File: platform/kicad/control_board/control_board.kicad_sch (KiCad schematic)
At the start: 39 parts, among them IC1 Adafruit_HUZZAH_ESP, J1 DHT22, J1 PoE 1, J1 RJ45 IN - 1, J10 USB_PWR_IN, J11 Barrel_Jack, J2 DS18B20, J2 PoE 2, J2 RJ45 IN - 2, J3 PoE 3, J3 RJ45 IN - 3, J3 Sensor1, J4 Sensor2, J6 24V IN, J7 24V/5V OUT, J8 Nav Light, K1 LCA717, K2 LCA717, K3 LCA717, K4 LCA717, M1 STEPDOWN->5V, U1 USB_A_2.0

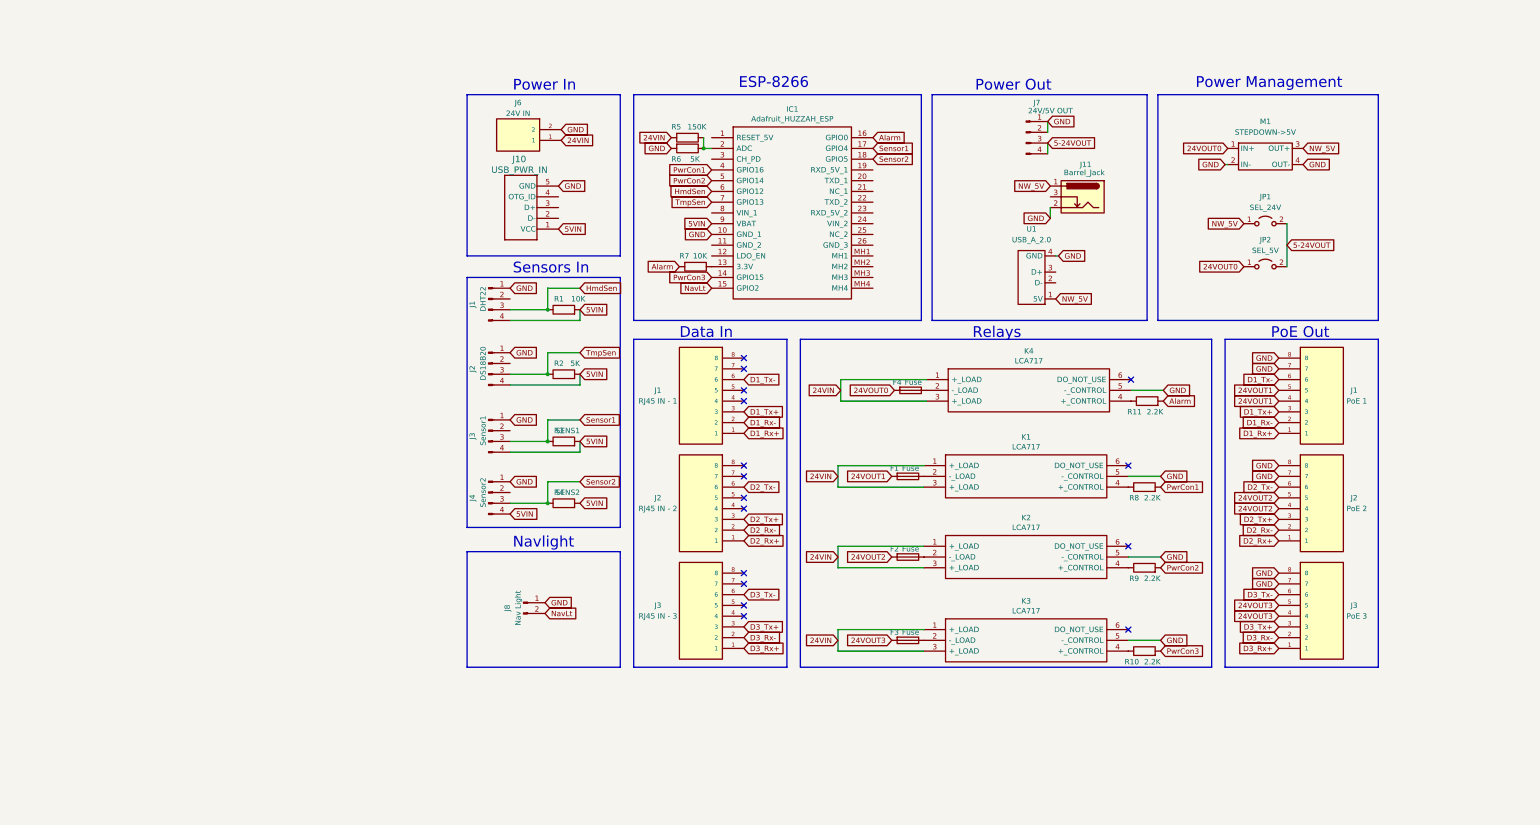
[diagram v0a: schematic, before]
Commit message: Control Board: Complete Schematic and Footprint assignment (#3)
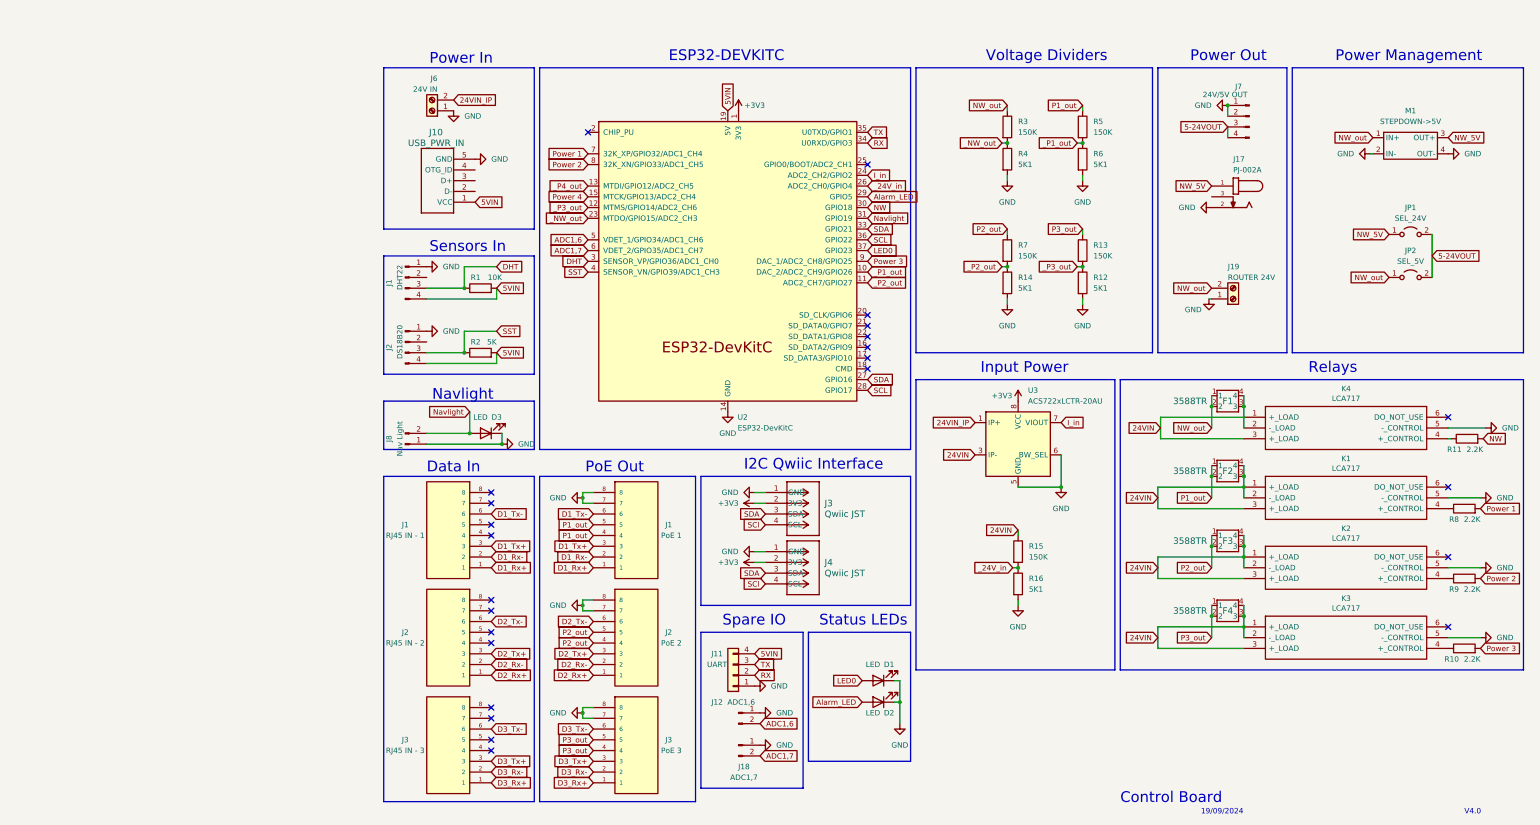
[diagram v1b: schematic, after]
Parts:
- removed F1, F2, F3, F4: Fuse, Fuse:Fuseholder_Blade_Mini_Keystone_3568, symbol Device:Fuse
- removed IC1: Adafruit_HUZZAH_ESP, Module:Adafruit_HUZZAH_ESP8266_breakout, symbol AusOceanPCB-rescue:Adafruit_HUZZAH_ESP-MISC
- removed J11: Barrel_Jack, AusOcean:3.5x1.35mm_Barrel_Jack_Port, symbol Connector:Barrel_Jack_Switch
- removed J3: Sensor1, Connector_JST:JST_EH_B4B-EH-A_1x04_P2.50mm_Vertical, symbol AusOceanPCB-rescue:Conn_01x04_Male-Connector
- removed J4: Sensor2, Connector_JST:JST_EH_B4B-EH-A_1x04_P2.50mm_Vertical, symbol AusOceanPCB-rescue:Conn_01x04_Male-Connector
- removed J6: 24V IN, AusOcean:CUI_Screw_terminal_1x2, symbol AusOcean:TB002-500-02BE
- removed U1: USB_A_2.0, AusOcean:USB_A_2.0_CONN, symbol AusOcean:USB_A_2.0
- added D1, D2, D3: LED, LED_SMD:LED_0603_1608Metric, symbol Device:LED
- added F1, F2, F3, F4: 3588TR, AusOcean:3588TR_FUSE_HOLDER, symbol AusOcean:3588TR
- added J11: UART, Connector_PinHeader_2.54mm:PinHeader_1x04_P2.54mm_Vertical, symbol Connector_Generic:Conn_01x04
- added J12: ADC1,6, Connector_PinHeader_2.54mm:PinHeader_1x02_P2.54mm_Vertical, symbol Connector:Conn_01x02_Pin
- added J17: PJ-002A, PJ-002A:CUI_PJ-002A, symbol AusOcean:PJ-002A
- added J18: ADC1,7, Connector_PinHeader_2.54mm:PinHeader_1x02_P2.54mm_Vertical, symbol Connector:Conn_01x02_Pin
- added J19: ROUTER 24V, AusOcean:CUI_Screw_terminal_1x2, symbol Connector:Screw_Terminal_01x02
- added J3, J4: Qwiic JST, AusOcean:CONN_SM04B-SRSS-TB_JST, symbol AusOcean:Qwiic JST
- added J6: 24V IN, AusOcean:CUI_Screw_terminal_1x2, symbol Connector:Screw_Terminal_01x02
- added R12, R14, R16: 5K1, Resistor_SMD:R_0201_0603Metric, symbol Device:R
- added R13, R15: 150K, Resistor_SMD:R_0201_0603Metric, symbol Device:R
- added U2: ESP32-DevKitC, Espressif:ESP32-DevKitC, symbol Espressif:ESP32-DevKitC
- added U3: ACS722xLCTR-20AU, Package_SO:SOIC-8_3.9x4.9mm_P1.27mm, symbol Sensor_Current:ACS722xLCTR-20AU
- R1, R10, R11, R2, R5, R8, R9: footprint Resistor_THT:R_Axial_DIN0207_L6.3mm_D2.5mm_P7.62mm_Horizontal -> Resistor_SMD:R_0201_0603Metric
- R3: value SENS1 -> 150K; footprint Resistor_THT:R_Axial_DIN0207_L6.3mm_D2.5mm_P7.62mm_Horizontal -> Resistor_SMD:R_0201_0603Metric
- R4: value SENS2 -> 5K1; footprint Resistor_THT:R_Axial_DIN0207_L6.3mm_D2.5mm_P7.62mm_Horizontal -> Resistor_SMD:R_0201_0603Metric
- R6: value 5K -> 5K1; footprint Resistor_THT:R_Axial_DIN0207_L6.3mm_D2.5mm_P7.62mm_Horizontal -> Resistor_SMD:R_0201_0603Metric
- R7: value 10K -> 150K; footprint Resistor_THT:R_Axial_DIN0207_L6.3mm_D2.5mm_P7.62mm_Horizontal -> Resistor_SMD:R_0201_0603Metric
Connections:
- net 24VOUT1 is gone; now on net P1_out: J1.4, J1.5
- net 24VOUT2 is gone; now on net P2_out: J2.4, J2.5
- net Sensor1 is gone; now on net NW_out: R3.1
- net 24VIN: now also K1.2 (-_LOAD), K2.2 (-_LOAD), K3.2 (-_LOAD), F2.3, F2.4, F3.3, F3.4, F4.3, F4.4, R15.1, U3.3 (IP-), U3.4 (IP-); no longer R5.2
- net 5VIN: now also J11.4 (Pin_4), U2.19 (5V); no longer R3.2, R4.2
- net GND: now also R4.2, D1.1 (K), D2.1 (K), D3.1 (K), J11.1 (Pin_1), J12.1 (Pin_1), J17.2, J18.1 (Pin_1), J19.1 (Pin_1), J3.1 (GND), J4.1 (GND), J6.1 (Pin_1), R12.2, R14.2, R16.2, U2.14 (GND), U2.32 (GND), U2.38 (GND), U3.5 (GND), U3.6 (BW_SEL)
- net NW_5V: now also J17.1
- net P2_out: now reaches R7.1
- net P2_out: now also F3.1, F3.2
- net at K4.2 (-_LOAD): now also F1.3, F1.4
- net P1_out: now reaches R5.1
- net P1_out: now also F2.1, F2.2; no longer R6.1
- net 24VOUT0 renamed NW_out
- net NW_out: now also F1.1, F1.2, J19.2 (Pin_2)
- net 24VOUT3 renamed P3_out
- net P3_out: now also F4.1, F4.2, R13.1
- net Alarm renamed NW
- net NW: now also U2.30 (GPIO18); no longer R7.2
- net HmdSen renamed DHT
- net DHT: now also U2.3 (SENSOR_VP/GPIO36/ADC1_CH0)
- net NavLt renamed Navlight
- net Navlight: now also D3.2 (A), U2.31 (GPIO19)
- net PwrCon1 renamed Power 1
- net Power 1: now also U2.7 (32K_XP/GPIO32/ADC1_CH4)
- net PwrCon2 renamed Power 2
- net Power 2: now also U2.8 (32K_XN/GPIO33/ADC1_CH5)
- net PwrCon3 renamed Power 3
- net Power 3: now also U2.9 (DAC_1/ADC2_CH8/GPIO25)
- net Sensor2 renamed _NW_out
- net _NW_out: now also R3.2, U2.23 (MTDO/GPIO15/ADC2_CH3)
- net TmpSen renamed SST
- net SST: now also U2.4 (SENSOR_VN/GPIO39/ADC1_CH3)
- new net +3V3: J3.2 (3V3), J4.2 (3V3), U2.1 (3V3), U3.8 (VCC)
- new net 24VIN_IP: J6.2 (Pin_2), U3.1 (IP+), U3.2 (IP+)
- new net ADC1,6: J12.2 (Pin_2), U2.5 (VDET_1/GPIO34/ADC1_CH6)
- new net ADC1,7: J18.2 (Pin_2), U2.6 (VDET_2/GPIO35/ADC1_CH7)
- new net Alarm_LED: D2.2 (A), U2.29 (GPIO5)
- new net I_in: U2.24 (ADC2_CH2/GPIO2), U3.7 (VIOUT)
- new net LED0: D1.2 (A), U2.37 (GPIO23)
- new net Power 4: U2.15 (MTCK/GPIO13/ADC2_CH4)
- new net RX: J11.2 (Pin_2), U2.34 (U0RXD/GPIO3)
- new net SCL: U2.28 (GPIO17), U2.36 (GPIO22)
- new net SCl: J3.4 (SCL), J4.4 (SCL)
- new net SDA: J3.3 (SDA), J4.3 (SDA), U2.27 (GPIO16), U2.33 (GPIO21)
- new net TX: J11.3 (Pin_3), U2.35 (U0TXD/GPIO1)
- new net _24V_in: R15.2, R16.1, U2.26 (ADC2_CH0/GPIO4)
- new net _P1_out: R5.2, R6.1, U2.10 (DAC_2/ADC2_CH9/GPIO26)
- new net _P2_out: R14.1, R7.2, U2.11 (ADC2_CH7/GPIO27)
- new net _P3_out: R12.1, R13.2, U2.12 (MTMS/GPIO14/ADC2_CH6)
- new net _P4_out: U2.13 (MTDI/GPIO12/ADC2_CH5)
- no-connect marks 16 -> 24
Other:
- note added: "19/09/2024"
- note added: "Control Board"
- note added: "ESP32-DEVKITC"
- note added: "I2C Qwiic Interface"
- note added: "Input Power"
- note added: "Spare IO"
- note added: "Status LEDs"
- note added: "V4.0"
- note added: "Voltage Dividers"
- note removed: "ESP-8266"
- moved on the sheet: J1, J10, J2, J3, J7, J8, JP1, JP2, K1, K2, K3, K4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

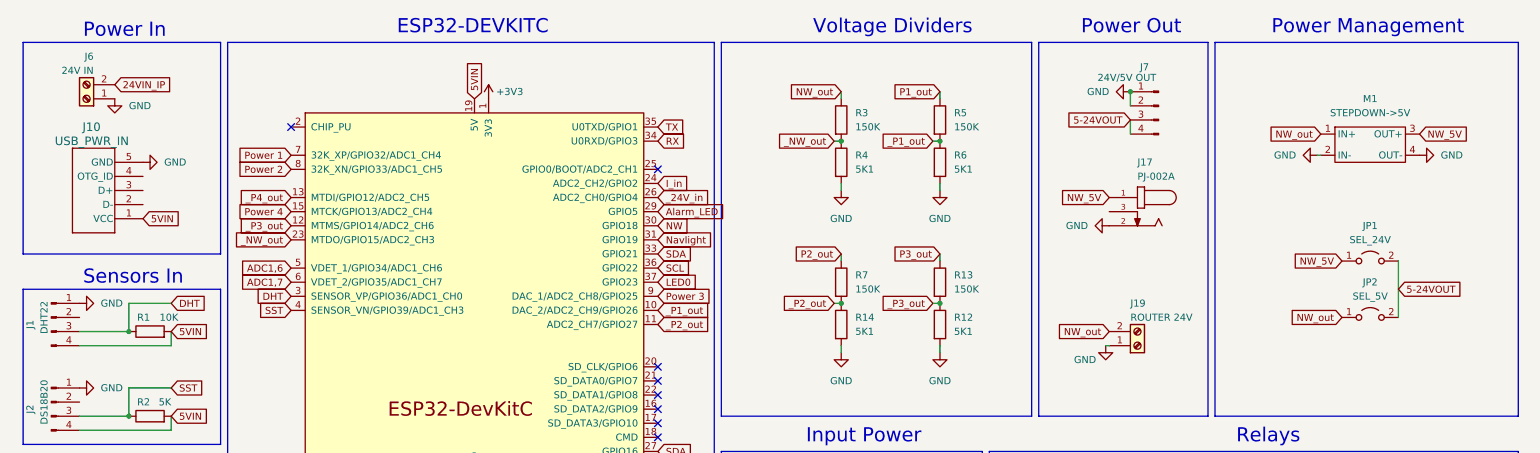
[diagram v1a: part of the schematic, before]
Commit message: Control Board: Add all 3d models and complete initial layout (#3)
This change adds a new models directory which contains the 3d models for the footprints used in PCBs.
This change also completes a draft layout for the new PCB.
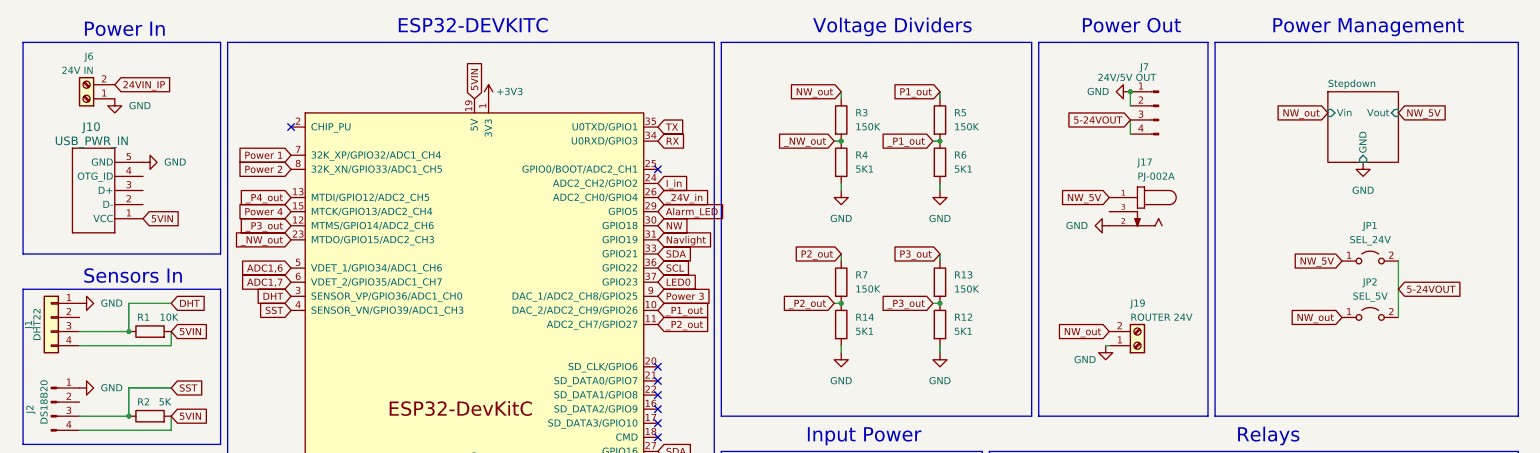
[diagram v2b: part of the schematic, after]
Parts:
- removed J1: DHT22, Connector_JST:JST_EH_B4B-EH-A_1x04_P2.50mm_Vertical, symbol AusOceanPCB-rescue:Conn_01x04_Male-Connector
- removed M1: STEPDOWN->5V, AusOcean:LM2596_Step_Down_Module, symbol AusOcean:LM2596_SD
- added J1: DHT22, Connector_PinHeader_2.54mm:PinHeader_1x04_P2.54mm_Horizontal, symbol Connector_Generic:Conn_01x04
- J17: footprint PJ-002A:CUI_PJ-002A -> AusOcean:CUI_PJ-002A
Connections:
- net 5VIN: now also J1.4 (Pin_4)
- net DHT: now also J1.3 (Pin_3)
- net GND: now also J1.1 (Pin_1)
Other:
- added sheet Stepdown (stepdown.kicad_sch)

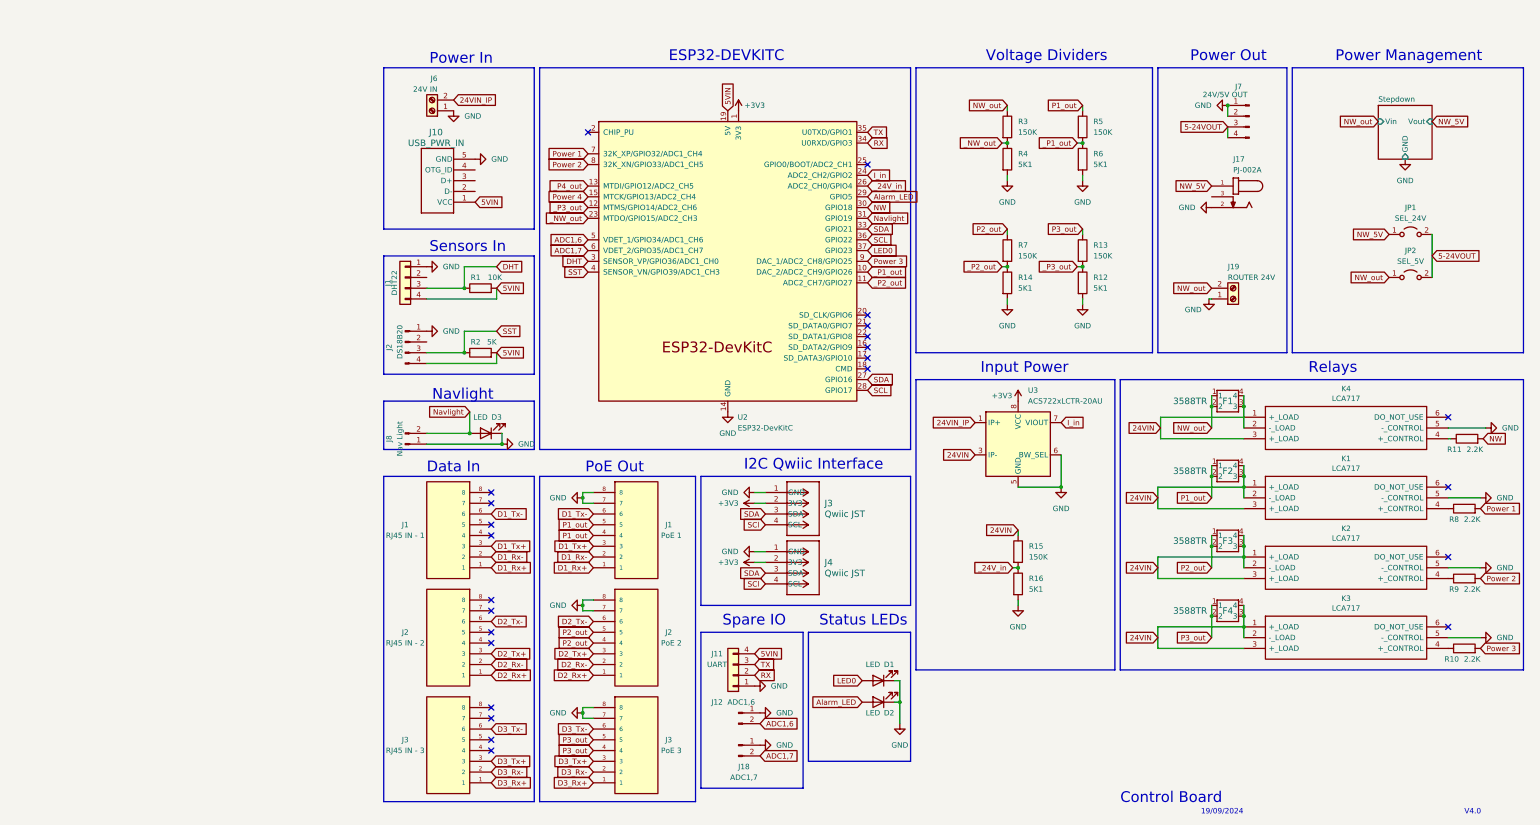
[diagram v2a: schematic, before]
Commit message: Control PCB: Update layout (#3)
This change updates the layout of the PCB to revise the feedback from the previous iteration.
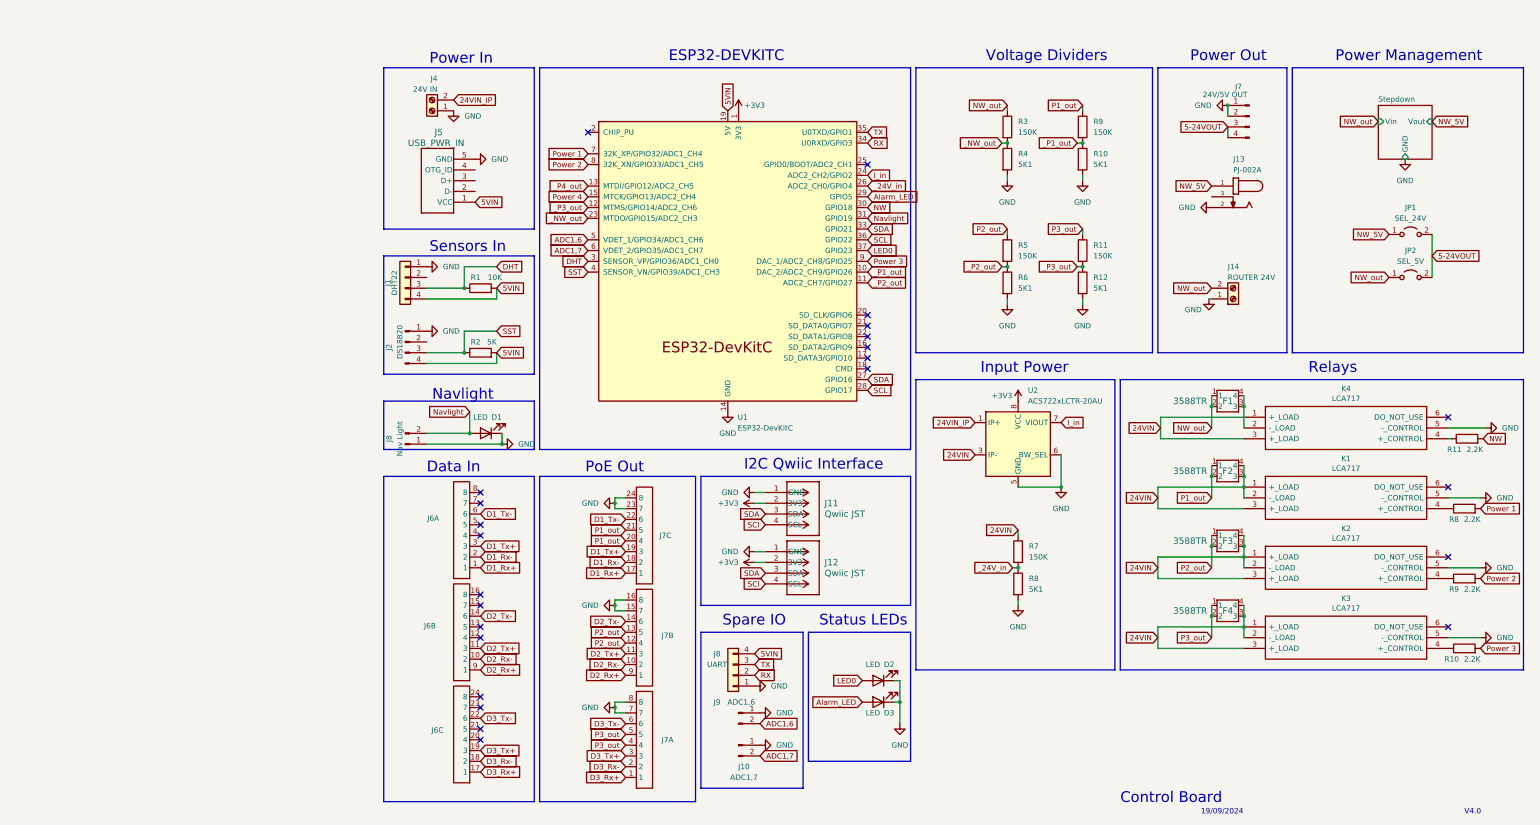
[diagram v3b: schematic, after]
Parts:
- removed J1: PoE 1, AusOcean:RJ45_Socket, symbol AusOcean:CRJ032-1-TH
- removed J1: RJ45 IN - 1, AusOcean:RJ45_Socket, symbol AusOcean:CRJ032-1-TH
- removed J2: PoE 2, AusOcean:RJ45_Socket, symbol AusOcean:CRJ032-1-TH
- removed J2: RJ45 IN - 2, AusOcean:RJ45_Socket, symbol AusOcean:CRJ032-1-TH
- removed J3: RJ45 IN - 3, AusOcean:RJ45_Socket, symbol AusOcean:CRJ032-1-TH
- removed J3: PoE 3, AusOcean:RJ45_Socket, symbol AusOcean:CRJ032-1-TH
- added J6, J7: ~, AusOcean:RJ45 3-port jack, symbol AusOcean:RJ45_3-port_jack
- added unit 2 of J7
- added unit 3 of J7
- renumbered D3 to D1, D1 to D2, D2 to D3, J18 to J10, J3 to J11, J4 to J12, J17 to J13, J19 to J14, J6 to J4, J10 to J5, J11 to J8, J12 to J9, R6 to R10, R13 to R11, R7 to R5, R14 to R6, R15 to R7, R16 to R8, R5 to R9, U2 to U1, U3 to U2
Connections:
- net D1_Rx+: now also J6.1, J7.17 (1)
- net D1_Rx-: now also J6.2, J7.18 (2)
- net D1_Tx+: now also J6.3, J7.19 (3)
- net D1_Tx-: now also J6.6, J7.22 (6)
- net D2_Rx+: now also J6.9 (1), J7.9 (1)
- net D2_Rx-: now also J6.10 (2), J7.10 (2)
- net D2_Tx+: now also J6.11 (3), J7.11 (3)
- net D2_Tx-: now also J6.14 (6), J7.14 (6)
- net D3_Rx+: now also J6.17 (1), J7.1
- net D3_Rx-: now also J6.18 (2), J7.2
- net D3_Tx+: now also J6.19 (3), J7.3
- net D3_Tx-: now also J6.22 (6), J7.6
- net GND: now also J7.15 (7), J7.16 (8), J7.23 (7), J7.24 (8), J7.7, J7.8
- net P1_out: now also J7.20 (4), J7.21 (5)
- net P2_out: now also J7.12 (4), J7.13 (5)
- net P3_out: now also J7.4, J7.5
